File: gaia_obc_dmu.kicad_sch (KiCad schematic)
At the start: 7 parts, among them J2 Micro_SD_Card_Det2, U7 WLR089U0-I_RM

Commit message: finishing psu
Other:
- moved on the sheet: U7
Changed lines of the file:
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@@
 	(symbol
 		(lib_id "cs25_onionsat:WLR089U0-I_RM")
-		(at 129.54 58.42 180)
+		(at 116.84 52.07 180)
 		(unit 1)
 		(exclude_from_sim no)
@@
 		(fields_autoplaced yes)
 		(property "Reference" "U7"
-			(at 129.54 25.4 0)
+			(at 116.84 19.05 0)
 			(effects
 				(font
@@
 		)
 		(property "Value" "WLR089U0-I_RM"
-			(at 129.54 27.94 0)
+			(at 116.84 21.59 0)
 			(effects
 				(font
@@
 		)
 		(property "Footprint" "OnionSAT_Gaia:MODULE_WLR089U0-I_RM"
-			(at 129.54 58.42 0)
+			(at 116.84 52.07 0)
 			(effects
 				(font
@@
 		)
 		(property "Datasheet" ""
-			(at 129.54 58.42 0)
+			(at 116.84 52.07 0)
 			(effects
 				(font
@@
 		)
 		(property "Description" ""
-			(at 129.54 58.42 0)
+			(at 116.84 52.07 0)
 			(effects
 				(font
@@
 		)
 		(property "MF" "Microchip Technology"
-			(at 129.54 58.42 0)
+			(at 116.84 52.07 0)
 			(effects
 				(font
@@
 		)
 		(property "MAXIMUM_PACKAGE_HEIGHT" "2.8mm"
-			(at 129.54 58.42 0)
+			(at 116.84 52.07 0)
 			(effects
 				(font
@@
 		)
 		(property "Package" "None"
-			(at 129.54 58.42 0)
+			(at 116.84 52.07 0)
 			(effects
 				(font
@@
 		)
 		(property "Price" "None"
-			(at 129.54 58.42 0)
+			(at 116.84 52.07 0)
 			(effects
 				(font
@@
 		)
 		(property "Check_prices" "https://www.snapeda.com/parts/WLR089U0IRM/Microchip/view-part/?ref=eda"
-			(at 129.54 58.42 0)
+			(at 116.84 52.07 0)
 			(effects
 				(font
@@
 		)
 		(property "STANDARD" "Manufacturer Recommendations"
-			(at 129.54 58.42 0)
+			(at 116.84 52.07 0)
 			(effects
 				(font
@@
 		)
 		(property "PARTREV" "B"
-			(at 129.54 58.42 0)
+			(at 116.84 52.07 0)
 			(effects
 				(font
@@
 		)
 		(property "SnapEDA_Link" "https://www.snapeda.com/parts/WLR089U0IRM/Microchip/view-part/?ref=snap"
-			(at 129.54 58.42 0)
+			(at 116.84 52.07 0)
 			(effects
 				(font
@@
 		)
 		(property "MP" "WLR089U0IRM"
-			(at 129.54 58.42 0)
+			(at 116.84 52.07 0)
 			(effects
 				(font
@@
 		)
 		(property "Description_1" "\n                        \n                            ULTRA-LOW POWER LONG RANGE LORA MODULE (863-928 MHZ) 41 MODULE 13.5X17MM TRAY;\n                        \n"
-			(at 129.54 58.42 0)
+			(at 116.84 52.07 0)
 			(effects
 				(font
@@
 		)
 		(property "Availability" "Not in stock"
-			(at 129.54 58.42 0)
+			(at 116.84 52.07 0)
 			(effects
 				(font
@@
 		)
 		(property "MANUFACTURER" "Microchip"
-			(at 129.54 58.42 0)
+			(at 116.84 52.07 0)
 			(effects
 				(font

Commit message: almost final release
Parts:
- removed R10, R11, R12, R9: 10k, symbol Device:R_Small
- removed U7: WLR089U0-I_RM, OnionSAT_Gaia:MODULE_WLR089U0-I_RM, symbol cs25_onionsat:WLR089U0-I_RM
- added C38, C40, C42: 100nF, Capacitor_SMD:C_0402_1005Metric, symbol Device:C_Small
- added C41: 1uF, Capacitor_SMD:C_0402_1005Metric, symbol Device:C_Small
- added D3: LED_Small, symbol Device:LED_Small
- added J6: Conn_Coaxial_Small, Connector_Coaxial:SMA_Amphenol_132134-10_Vertical, symbol Connector:Conn_Coaxial_Small
- added Q2: BSS138, Package_TO_SOT_SMD:SOT-23, symbol Transistor_FET:BSS138
- added R46, R47: 470, symbol Device:R_Small
- added R48: R_Small, symbol Device:R_Small
- added R49, R51, R52, R53, R54, R55: 10k, symbol Device:R_Small
- added R50: 10, symbol Device:R_Small
- added SW3, SW4, SW5, SW6, SW7: SW_Push, symbol Switch:SW_Push
- added U15: CD-PA1616, gaia_obc-footprints:XCVR_CD-PA1616D, symbol gaia_obc-symbols:CD-PA1616
- added U16: RFM95W-868S2, RF_Module:HOPERF_RFM9XW_SMD, symbol RF_Module:RFM95W-868S2
- added U17: ~, symbol gaia_obc-symbols:kepernyo
- C39: renamed from C5; footprint (none) -> Capacitor_SMD:C_0402_1005Metric
- renumbered J2 to J5
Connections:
- net +3.3V: now also C38.1, C40.2, C41.2, SW3.2, SW4.2, SW5.2, SW6.2, SW7.2, U15.1 (VCC), U16.13 (3.3V)
- net GND: now also C38.2, C40.1, C41.1, C42.1, J6.1 (In), Q2.2 (S), R48.2, R51.1, R52.1, R53.1, R54.1, R55.1, U15.12 (GND), U15.19 (GND), U15.3 (GND), U15.8 (GND), U16.1 (GND), U16.10 (GND), U16.8 (GND), U17.13 (GND), U17.8 (GND)
- net SPI_CLK renamed SPI_0_SCLK
- net SPI_0_SCLK: now also U16.4 (SCK)
- net SPI_MISO renamed SPI_0_MISO
- net SPI_0_MISO: now also U16.2 (MISO)
- net SPI_MOSI renamed SPI_0_MOSI
- net SPI_0_MOSI: now also U16.3 (MOSI)
- new net: J6.2 (Ext), U16.9 (ANT)
- new net: R47.1, U15.10 (RX)
- new net: U15.16 (NC), U15.17 (NC), U15.18 (NC), U15.20 (NC), U15.6 (NC), U15.7 (NC)
- new net: D3.2 (A), U15.5 (3D-FIX)
- new net: R46.2, U15.9 (TX)
- new net: Q2.3 (D), R50.1
- new net: R50.2, U17.11 (LEDK)
- new net: D3.1 (K), R48.1
- new net: Q2.1 (G), R49.2
- new net +3V0: C42.2, R49.1, U17.10 (VCC), U17.12 (LEDA)
- new net GPS_RX: R47.2
- new net GPS_TX: R46.1
- new net LORA_CS: U16.5 (NSS)
- new net LORA_RESET: U16.6 (RESET)
- new net PB1: R51.2, SW3.1
- new net PB2: R52.2, SW4.1
- new net PB3: R53.2, SW5.1
- new net PB4: R54.2, SW6.1
- new net PB5: R55.2, SW7.1
- new net SCREEN_CLK: U17.4 (SCL)
- new net SCREEN_CS: U17.7 (CS)
- new net SCREEN_DC: U17.5 (RS)
- new net SCREEN_MOSI: U17.3 (SDA)
- new net SCREEN_RESET: U17.6 (RES)
- no-connect marks 5 -> 16
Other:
- moved on the sheet: C39, J5

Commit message: prep for routing 2/1
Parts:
- D3: footprint (none) -> LED_SMD:LED_0603_1608Metric
- SW3, SW4, SW5, SW6, SW7: footprint (none) -> Button_Switch_SMD:SW_SPST_PTS647_Sx50
- U17: footprint (none) -> gaia_obc-footprints:kepernyo
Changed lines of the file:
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@@
 			)
 		)
-		(property "Footprint" ""
+		(property "Footprint" "Button_Switch_SMD:SW_SPST_PTS647_Sx50"
 			(at 241.3 30.48 0)
 			(effects
@@
 			)
 		)
-		(property "Footprint" ""
+		(property "Footprint" "Button_Switch_SMD:SW_SPST_PTS647_Sx50"
 			(at 241.3 44.45 0)
 			(effects
@@
 			)
 		)
-		(property "Footprint" ""
+		(property "Footprint" "Button_Switch_SMD:SW_SPST_PTS647_Sx50"
 			(at 241.3 58.42 0)
 			(effects
@@
 			)
 		)
-		(property "Footprint" ""
+		(property "Footprint" "LED_SMD:LED_0603_1608Metric"
 			(at 91.44 96.52 90)
 			(effects
@@
 			)
 		)
-		(property "Footprint" ""
+		(property "Footprint" "Button_Switch_SMD:SW_SPST_PTS647_Sx50"
 			(at 241.3 73.66 0)
 			(effects
@@
 			)
 		)
-		(property "Footprint" ""
+		(property "Footprint" "gaia_obc-footprints:kepernyo"
 			(at 199.39 46.99 0)
 			(effects
@@
 			)
 		)
-		(property "Footprint" ""
+		(property "Footprint" "Button_Switch_SMD:SW_SPST_PTS647_Sx50"
 			(at 241.3 88.9 0)
 			(effects

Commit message: almost routeable//98% done schema
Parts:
- R55: renamed from R46; footprint (none) -> Resistor_SMD:R_0402_1005Metric
- R56: renamed from R47; footprint (none) -> Resistor_SMD:R_0402_1005Metric
- R57: renamed from R48; footprint (none) -> Resistor_SMD:R_0402_1005Metric
- R58: renamed from R49; footprint (none) -> Resistor_SMD:R_0402_1005Metric
- R59: renamed from R50; footprint (none) -> Resistor_SMD:R_0603_1608Metric
- R60: renamed from R51; footprint (none) -> Resistor_SMD:R_0402_1005Metric
- R61: renamed from R52; footprint (none) -> Resistor_SMD:R_0402_1005Metric
- R62: renamed from R53; footprint (none) -> Resistor_SMD:R_0402_1005Metric
- R63: renamed from R54; footprint (none) -> Resistor_SMD:R_0402_1005Metric
- R64: renamed from R55; footprint (none) -> Resistor_SMD:R_0402_1005Metric
- renumbered D3 to D12
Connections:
- no-connect marks 16 -> 17

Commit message: start routing
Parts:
- SW3, SW4, SW5, SW6, SW7: footprint Button_Switch_SMD:SW_SPST_PTS647_Sx50 -> gaia_obc-footprints:KEY-SMD_4P-L3.1-W3.1-P2.00-LS4.0
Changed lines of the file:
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@@
 			)
 		)
-		(property "Footprint" "Button_Switch_SMD:SW_SPST_PTS647_Sx50"
+		(property "Footprint" "gaia_obc-footprints:KEY-SMD_4P-L3.1-W3.1-P2.00-LS4.0"
 			(at 241.3 30.48 0)
 			(effects
@@
 			)
 		)
-		(property "Footprint" "Button_Switch_SMD:SW_SPST_PTS647_Sx50"
+		(property "Footprint" "gaia_obc-footprints:KEY-SMD_4P-L3.1-W3.1-P2.00-LS4.0"
 			(at 241.3 44.45 0)
 			(effects
@@
 			)
 		)
-		(property "Footprint" "Button_Switch_SMD:SW_SPST_PTS647_Sx50"
+		(property "Footprint" "gaia_obc-footprints:KEY-SMD_4P-L3.1-W3.1-P2.00-LS4.0"
 			(at 241.3 58.42 0)
 			(effects
@@
 			)
 		)
-		(property "Footprint" "Button_Switch_SMD:SW_SPST_PTS647_Sx50"
+		(property "Footprint" "gaia_obc-footprints:KEY-SMD_4P-L3.1-W3.1-P2.00-LS4.0"
 			(at 241.3 73.66 0)
 			(effects
@@
 			)
 		)
-		(property "Footprint" "Button_Switch_SMD:SW_SPST_PTS647_Sx50"
+		(property "Footprint" "gaia_obc-footprints:KEY-SMD_4P-L3.1-W3.1-P2.00-LS4.0"
 			(at 241.3 88.9 0)
 			(effects

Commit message: change screen
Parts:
- added C43, C44: 100nF, Capacitor_SMD:C_0402_1005Metric, symbol Device:C_Small
- added U18: BME280, Package_LGA:Bosch_LGA-8_2.5x2.5mm_P0.65mm_ClockwisePinNumbering, symbol Sensor:BME280
- J6: footprint Connector_Coaxial:SMA_Amphenol_132134-10_Vertical -> Connector_Coaxial:SMA_Amphenol_132134_Vertical
- U17: footprint gaia_obc-footprints:kepernyo -> gaia_obc-footprints:OLED-SMD_ST7735S
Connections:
- net +3.3V: now also C43.1, C44.1, U18.2 (CSB), U18.6 (VDDIO), U18.8 (VDD)
- net GND: now also J5.11 (SHIELD), C43.2, C44.2, U18.1 (GND), U18.5 (SDO), U18.7 (GND)
- new net I2C_1_SCL: U18.4 (SCK)
- new net I2C_1_SDA: U18.3 (SDI)
- no-connect marks 17 -> 16
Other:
- moved on the sheet: C42, J5, Q2, R58, R59, R60, R61, R62, R63, R64, SW3, SW4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

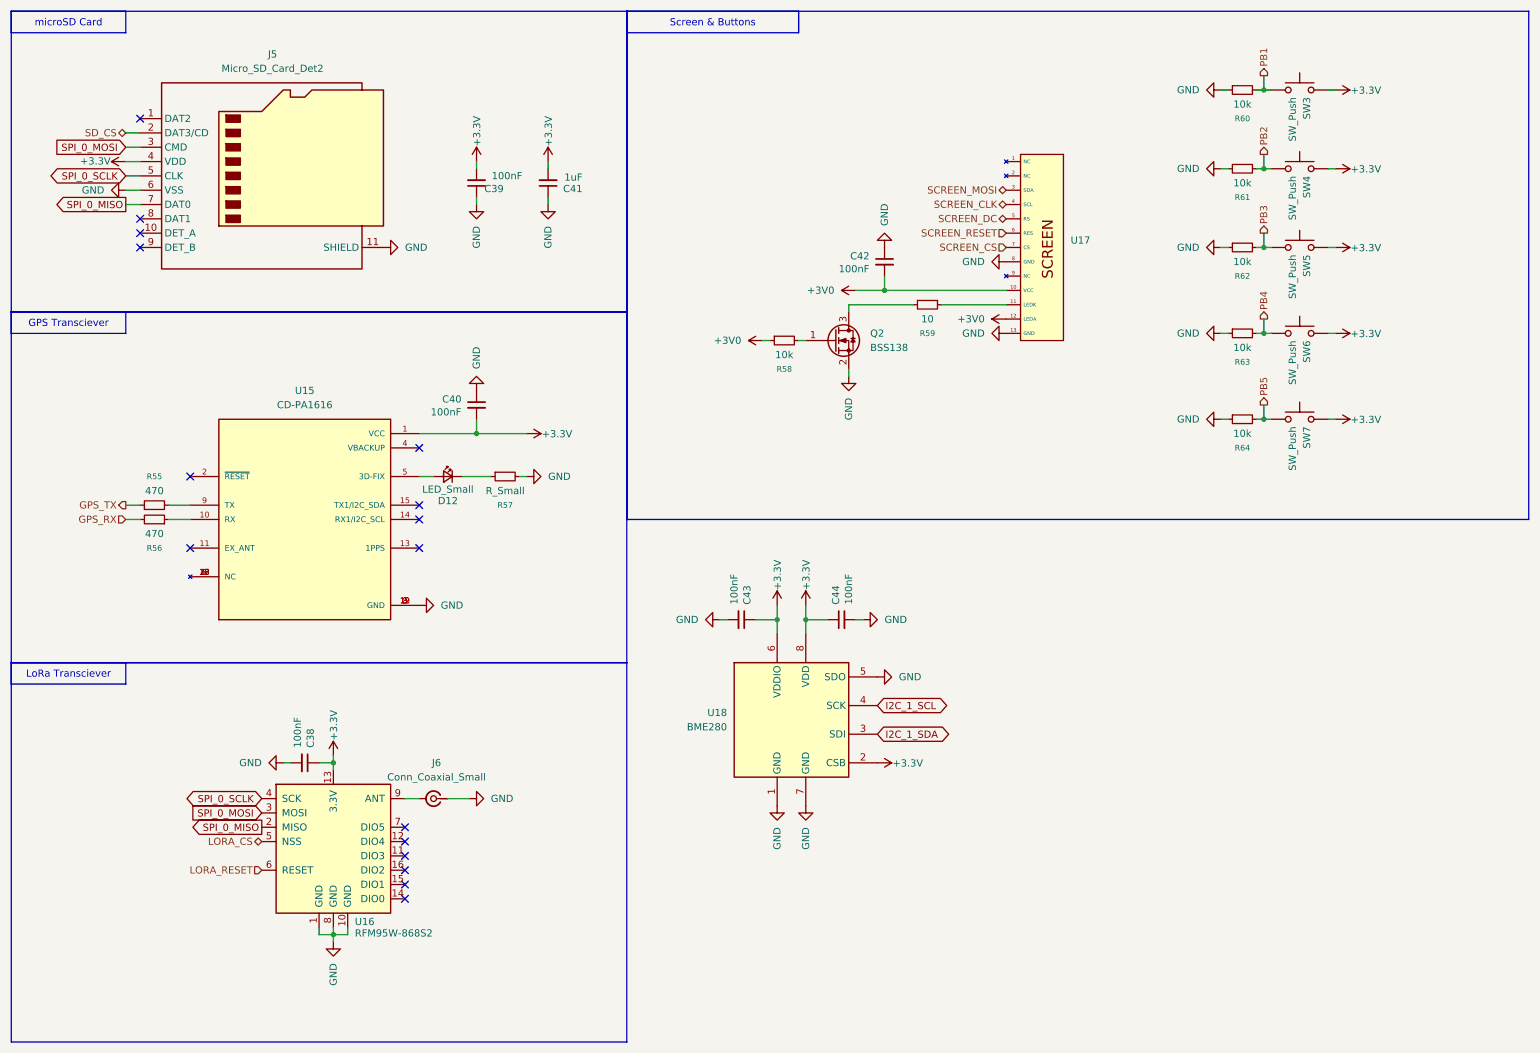
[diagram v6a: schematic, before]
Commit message: Finalizing schematic+Start placing components
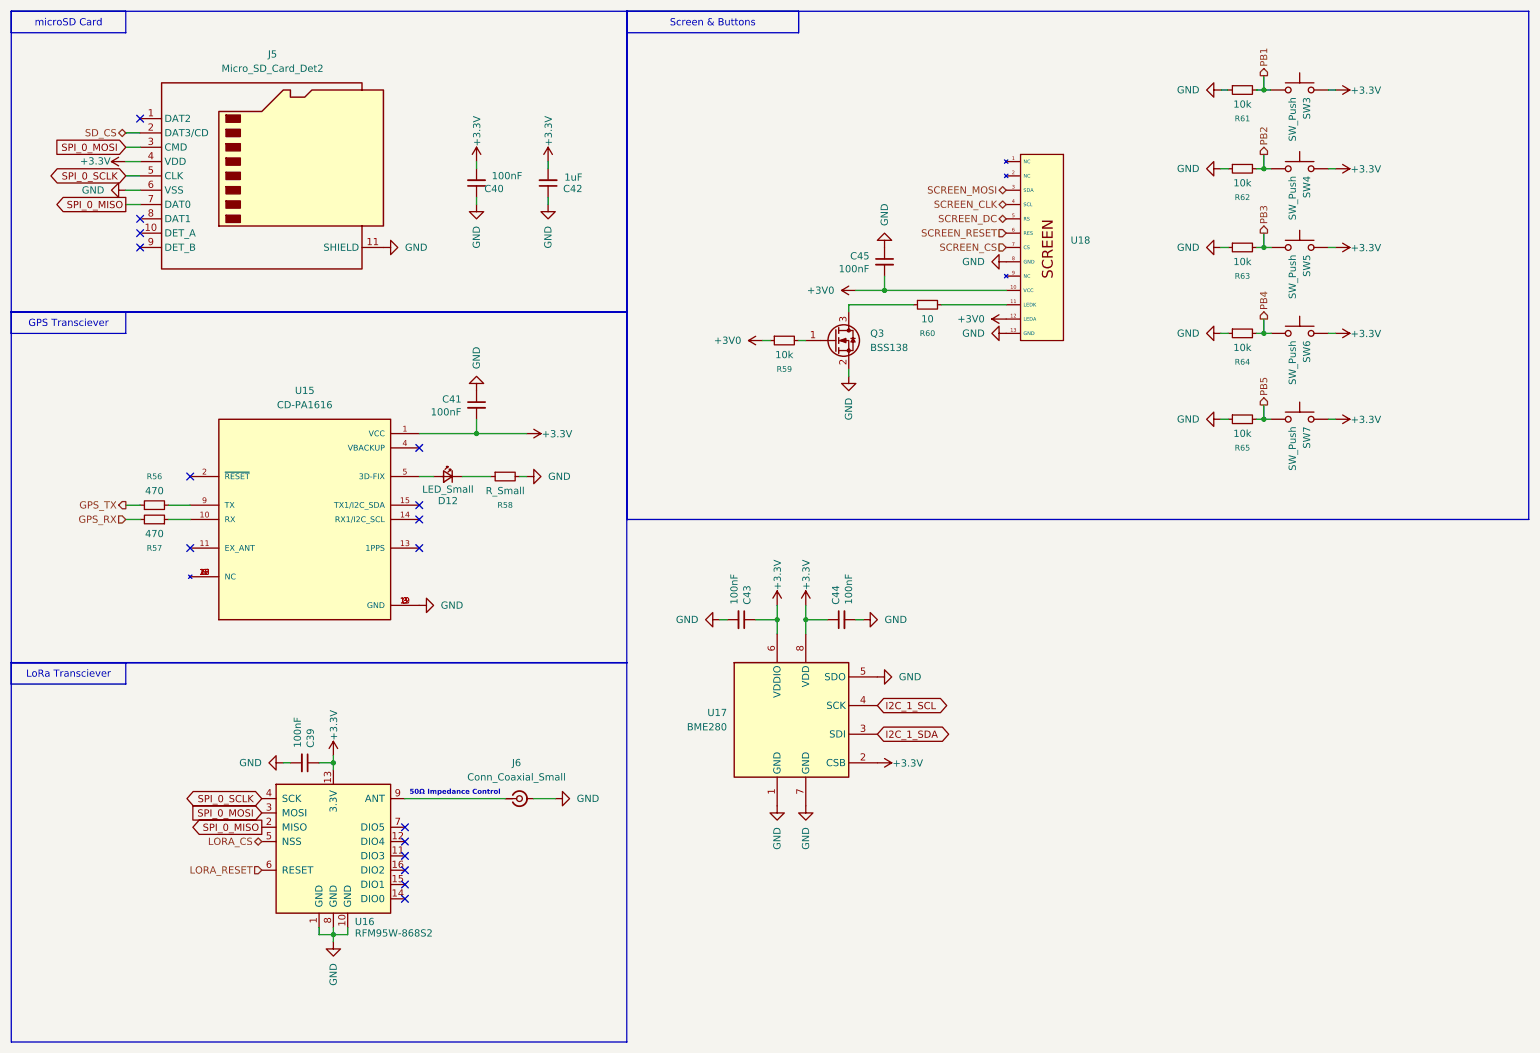
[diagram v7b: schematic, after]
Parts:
- renumbered C38 to C39, C39 to C40, C40 to C41, C41 to C42, C42 to C45, Q2 to Q3, R55 to R56, R56 to R57, R57 to R58, R58 to R59, R59 to R60, R60 to R61, R61 to R62, R62 to R63, R63 to R64, R64 to R65, U18 to U17, U17 to U18
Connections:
- net GND: now also J6.2 (Ext); no longer J6.1 (In)
- net at U16.9 (ANT): now also J6.1 (In); no longer J6.2 (Ext)
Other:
- note added: "50Ω Impedance Control"
- moved on the sheet: J6

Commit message: finish placing components+small fixes in schema
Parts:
- removed C45: 100nF, Capacitor_SMD:C_0402_1005Metric, symbol Device:C_Small
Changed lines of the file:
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@@
 		(color 0 0 0 0)
 	)
-	(junction
-		(at 168.91 63.5)
-		(diameter 0)
-		(color 0 0 0 0)
-	)
 	(no_connect
 		(at 36.83 55.88)
@@
 	(wire
 		(pts
-			(xy 168.91 63.5) (xy 190.5 63.5)
+			(xy 163.83 63.5) (xy 190.5 63.5)
 		)
 		(stroke
@@
 	(wire
 		(pts
-			(xy 168.91 60.96) (xy 168.91 63.5)
-		)
-		(stroke
-			(width 0)
-			(type default)
-		)
-	)
-	(wire
-		(pts
 			(xy 96.52 48.26) (xy 96.52 46.99)
 		)
@@
 	(wire
 		(pts
-			(xy 163.83 63.5) (xy 168.91 63.5)
-		)
-		(stroke
-			(width 0)
-			(type default)
-		)
-	)
-	(wire
-		(pts
 			(xy 41.91 104.14) (xy 45.72 104.14)
 		)
@@
 	(symbol
 		(lib_id "power:GND")
-		(at 168.91 55.88 180)
-		(unit 1)
-		(exclude_from_sim no)
-		(in_bom yes)
-		(on_board yes)
-		(dnp no)
-		(property "Reference" "#PWR0161"
-			(at 168.91 49.53 0)
-			(effects
-				(font
-					(size 1.27 1.27)
-				)
-				(hide yes)
-			)
-		)
-		(property "Value" "GND"
-			(at 168.91 52.07 90)
-			(effects
-				(font
-					(size 1.27 1.27)
-				)
-				(justify right)
-			)
-		)
-		(property "Footprint" ""
-			(at 168.91 55.88 0)
-			(effects
-				(font
-					(size 1.27 1.27)
-				)
-				(hide yes)
-			)
-		)
-		(property "Datasheet" ""
-			(at 168.91 55.88 0)
-			(effects
-				(font
-					(size 1.27 1.27)
-				)
-				(hide yes)
-			)
-		)
-		(property "Description" "Power symbol creates a global label with name \"GND\" , ground"
-			(at 168.91 55.88 0)
-			(effects
-				(font
-					(size 1.27 1.27)
-				)
-				(hide yes)
-			)
-		)
-		(pin "1"
-		)
-		(instances
-			(project "gaia_obc"
-				(path "/049f7784-e0f9-4d41-b308-330ac61e4408/fbf62360-00e1-4059-a494-d7d297b53182"
-					(reference "#PWR0161")
-					(unit 1)
-				)
-			)
-		)
-	)
-	(symbol
-		(lib_id "power:GND")
 		(at 110.49 153.67 90)
 		(unit 1)
@@
 					(unit 1)
 				)
-			)
-		)
-	)
-	(symbol
-		(lib_id "Device:C_Small")
-		(at 168.91 58.42 0)
-		(unit 1)
-		(exclude_from_sim no)
-		(in_bom yes)
-		(on_board yes)
-		(dnp no)
-		(property "Reference" "C45"
-			(at 162.814 57.404 0)
-			(effects
-				(font
-					(size 1.27 1.27)
-				)
-				(justify left)
-			)
-		)
-		(property "Value" "100nF"
-			(at 160.782 59.69 0)
-			(effects
-				(font
-					(size 1.27 1.27)
-				)
-				(justify left)
-			)
-		)
-		(property "Footprint" "Capacitor_SMD:C_0402_1005Metric"
-			(at 168.91 58.42 0)
-			(effects
-				(font
-					(size 1.27 1.27)
-				)
-				(hide yes)
-			)
-		)
-		(property "Datasheet" "~"
-			(at 168.91 58.42 0)
-			(effects
-				(font
-					(size 1.27 1.27)
-				)
-				(hide yes)
-			)
-		)
-		(property "Description" "Unpolarized capacitor, small symbol"
-			(at 168.91 58.42 0)
-			(effects
-				(font
-					(size 1.27 1.27)
-				)
-				(hide yes)
-			)
-		)
-		(pin "2"
-		)
-		(pin "1"
-		)
-		(instances
-			(project "gaia_obc"
-				(path "/049f7784-e0f9-4d41-b308-330ac61e4408/fbf62360-00e1-4059-a494-d7d297b53182"
-					(reference "C45")
-					(unit 1)
-				)
